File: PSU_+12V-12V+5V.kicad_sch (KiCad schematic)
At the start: 39 parts, among them Q1 BC557, Q2 BC557, Q3 BC547, Q4 BC547, U1 LM317L, U2 LM317L

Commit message: ...
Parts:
- added J1: Screw_Terminal_01x06, TerminalBlock_Phoenix:TerminalBlock_Phoenix_MKDS-1,5-6_1x06_P5.00mm_Horizontal, symbol Connector:Screw_Terminal_01x06
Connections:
- net at C13.1, D5.2 (A), D7.1 (K)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: now also J1.1 (Pin_1)
- net at C11.2, C13.2, C3.2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: now also J1.2 (Pin_2)
- net at C10.2, C12.2, C14.2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: now also J1.4 (Pin_4)
- net at C14.1, D6.2 (A), D8.1 (K)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: now also J1.3 (Pin_3)
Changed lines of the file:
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@@
   (junction (at 93.345 118.11) (diameter 0) (color 0 0 0 0)
   )
+  (junction (at 153.67 78.105) (diameter 0) (color 0 0 0 0)
+  )
   (junction (at 127.635 78.105) (diameter 0) (color 0 0 0 0)
   )
+  (junction (at 153.67 40.64) (diameter 0) (color 0 0 0 0)
+  )
   (junction (at 84.455 128.27) (diameter 0) (color 0 0 0 0)
   )
@@
   (junction (at 105.41 110.49) (diameter 0) (color 0 0 0 0)
   )
+  (junction (at 153.67 147.955) (diameter 0) (color 0 0 0 0)
+  )
   (junction (at 136.525 128.27) (diameter 0) (color 0 0 0 0)
   )
@@
   (junction (at 114.935 40.64) (diameter 0) (color 0 0 0 0)
   )
+  (junction (at 153.67 110.49) (diameter 0) (color 0 0 0 0)
+  )
   (junction (at 100.33 147.955) (diameter 0) (color 0 0 0 0)
   )
@@
     (stroke (width 0) (type default) (color 0 0 0 0))
   )
+  (wire (pts (xy 174.625 147.955) (xy 174.625 73.66))
+    (stroke (width 0) (type default) (color 0 0 0 0))
+  )
   (wire (pts (xy 76.2 95.25) (xy 76.2 87.63))
     (stroke (width 0) (type default) (color 0 0 0 0))
@@
     (stroke (width 0) (type default) (color 0 0 0 0))
   )
+  (wire (pts (xy 153.67 40.64) (xy 166.37 40.64))
+    (stroke (width 0) (type default) (color 0 0 0 0))
+  )
   (wire (pts (xy 106.68 139.065) (xy 106.68 147.955))
     (stroke (width 0) (type default) (color 0 0 0 0))
@@
     (stroke (width 0) (type default) (color 0 0 0 0))
   )
+  (wire (pts (xy 166.37 68.58) (xy 189.23 68.58))
+    (stroke (width 0) (type default) (color 0 0 0 0))
+  )
   (wire (pts (xy 114.935 147.955) (xy 127.635 147.955))
     (stroke (width 0) (type default) (color 0 0 0 0))
   )
+  (wire (pts (xy 166.37 66.04) (xy 189.23 66.04))
+    (stroke (width 0) (type default) (color 0 0 0 0))
+  )
   (wire (pts (xy 46.355 97.79) (xy 76.2 97.79))
     (stroke (width 0) (type default) (color 0 0 0 0))
@@
     (stroke (width 0) (type default) (color 0 0 0 0))
   )
+  (wire (pts (xy 169.545 110.49) (xy 169.545 71.12))
+    (stroke (width 0) (type default) (color 0 0 0 0))
+  )
   (wire (pts (xy 136.525 48.895) (xy 136.525 40.64))
     (stroke (width 0) (type default) (color 0 0 0 0))
@@
     (stroke (width 0) (type default) (color 0 0 0 0))
   )
+  (wire (pts (xy 174.625 73.66) (xy 189.23 73.66))
+    (stroke (width 0) (type default) (color 0 0 0 0))
+  )
   (wire (pts (xy 106.68 147.955) (xy 114.935 147.955))
     (stroke (width 0) (type default) (color 0 0 0 0))
@@
     (stroke (width 0) (type default) (color 0 0 0 0))
   )
+  (wire (pts (xy 153.67 110.49) (xy 169.545 110.49))
+    (stroke (width 0) (type default) (color 0 0 0 0))
+  )
   (wire (pts (xy 46.355 105.41) (xy 60.96 105.41))
     (stroke (width 0) (type default) (color 0 0 0 0))
   )
+  (wire (pts (xy 153.67 78.105) (xy 166.37 78.105))
+    (stroke (width 0) (type default) (color 0 0 0 0))
+  )
   (wire (pts (xy 46.355 95.25) (xy 76.2 95.25))
     (stroke (width 0) (type default) (color 0 0 0 0))
@@
     (stroke (width 0) (type default) (color 0 0 0 0))
   )
+  (wire (pts (xy 166.37 78.105) (xy 166.37 68.58))
+    (stroke (width 0) (type default) (color 0 0 0 0))
+  )
+  (wire (pts (xy 169.545 71.12) (xy 189.23 71.12))
+    (stroke (width 0) (type default) (color 0 0 0 0))
+  )
   (wire (pts (xy 127.635 128.27) (xy 136.525 128.27))
     (stroke (width 0) (type default) (color 0 0 0 0))
@@
     (stroke (width 0) (type default) (color 0 0 0 0))
   )
+  (wire (pts (xy 153.67 147.955) (xy 174.625 147.955))
+    (stroke (width 0) (type default) (color 0 0 0 0))
+  )
   (wire (pts (xy 106.68 58.42) (xy 106.68 64.135))
     (stroke (width 0) (type default) (color 0 0 0 0))
@@
   )
   (wire (pts (xy 114.935 78.105) (xy 127.635 78.105))
+    (stroke (width 0) (type default) (color 0 0 0 0))
+  )
+  (wire (pts (xy 166.37 40.64) (xy 166.37 66.04))
     (stroke (width 0) (type default) (color 0 0 0 0))
   )
@@
     (pin "2")
   )
+  (symbol (lib_id "Connector:Screw_Terminal_01x06") (at 194.31 71.12 0) (unit 1)
+    (in_bom yes) (on_board yes) (fields_autoplaced)
+    (property "Reference" "J1" (id 0) (at 196.85 71.1199 0)
+      (effects (font (size 1.27 1.27)) (justify left))
+    )
+    (property "Value" "Screw_Terminal_01x06" (id 1) (at 196.85 73.6599 0)
+      (effects (font (size 1.27 1.27)) (justify left))
+    )
+    (property "Footprint" "TerminalBlock_Phoenix:TerminalBlock_Phoenix_MKDS-1,5-6_1x06_P5.00mm_Horizontal" (id 2) (at 194.31 71.12 0)
+      (effects (font (size 1.27 1.27)) hide)
+    )
+    (property "Datasheet" "~" (id 3) (at 194.31 71.12 0)
+      (effects (font (size 1.27 1.27)) hide)
+    )
+    (pin "1")
+    (pin "2")
+    (pin "3")
+    (pin "4")
+    (pin "5")
+    (pin "6")
+  )
   (symbol (lib_id "Device:R_Small") (at 106.68 66.675 180) (unit 1)
     (in_bom yes) (on_board yes)
@@
       (reference "D8") (unit 1) (value "1N4004") (footprint "Diode_THT:D_DO-41_SOD81_P10.16mm_Horizontal")
     )
+    (path "/c78bdea5-e185-4052-a5d1-0feec00b8a09"
+      (reference "J1") (unit 1) (value "Screw_Terminal_01x06") (footprint "TerminalBlock_Phoenix:TerminalBlock_Phoenix_MKDS-1,5-6_1x06_P5.00mm_Horizontal")
+    )
     (path "/961e5191-6ef0-485b-8715-bf0eec14a118"

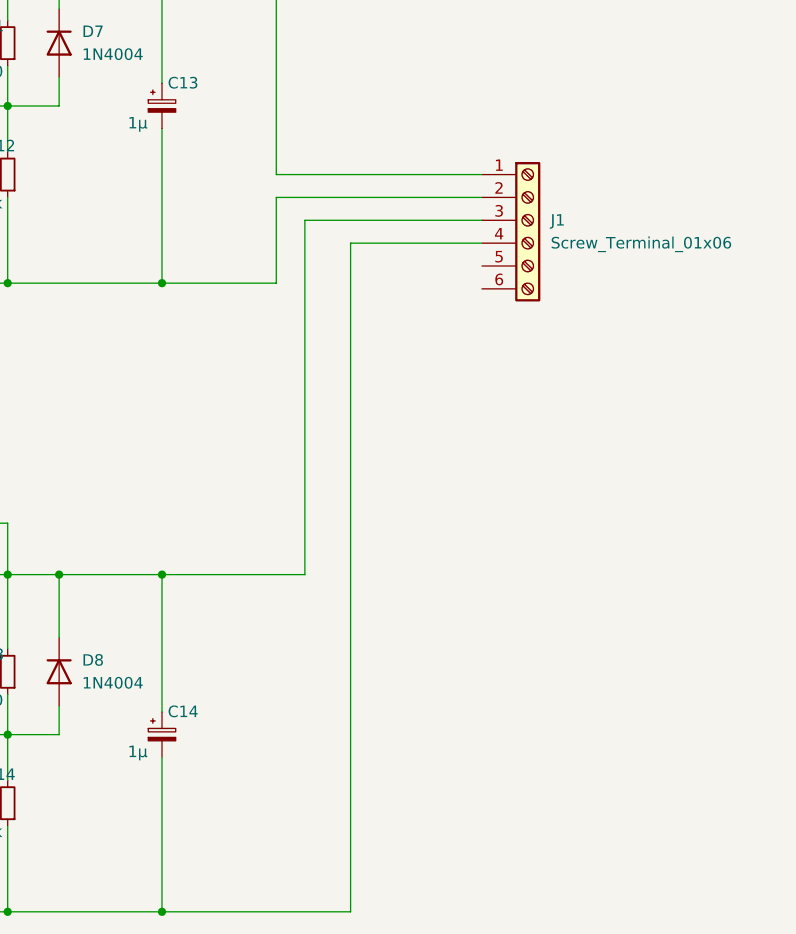
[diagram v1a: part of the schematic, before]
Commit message: Herschikkingen om filled area te optimaizeren
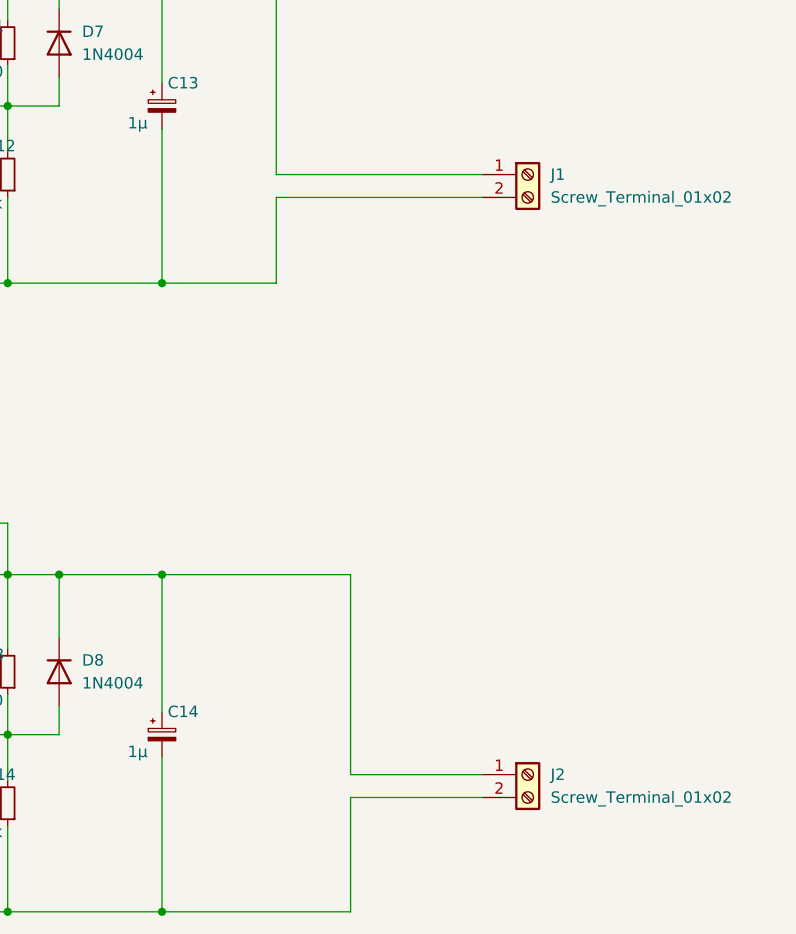
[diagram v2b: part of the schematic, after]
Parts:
- removed J1: Screw_Terminal_01x06, TerminalBlock_Phoenix:TerminalBlock_Phoenix_MKDS-1,5-6_1x06_P5.00mm_Horizontal, symbol Connector:Screw_Terminal_01x06
- added J1, J2: Screw_Terminal_01x02, TerminalBlock_Phoenix:TerminalBlock_Phoenix_MKDS-1,5-2_1x02_P5.00mm_Horizontal, symbol Connector:Screw_Terminal_01x02
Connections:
- net at C13.1, D5.2 (A), D7.1 (K)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: now also J1.1 (Pin_1)
- net at C11.2, C13.2, C3.2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: now also J1.2 (Pin_2)
- net at C10.2, C12.2, C14.2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: now also J2.2 (Pin_2)
- net at C14.1, D6.2 (A), D8.1 (K)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: now also J2.1 (Pin_1)
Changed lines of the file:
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@@
+    (stroke (width 0) (type default) (color 0 0 0 0))
+  )
+  (wire (pts (xy 174.625 132.715) (xy 174.625 110.49))
     (stroke (width 0) (type default) (color 0 0 0 0))
   )
@@
     (stroke (width 0) (type default) (color 0 0 0 0))
   )
-  (wire (pts (xy 174.625 147.955) (xy 174.625 73.66))
-    (stroke (width 0) (type default) (color 0 0 0 0))
-  )
   (wire (pts (xy 76.2 95.25) (xy 76.2 87.63))
     (stroke (width 0) (type default) (color 0 0 0 0))
@@
     (stroke (width 0) (type default) (color 0 0 0 0))
   )
+  (wire (pts (xy 174.625 147.955) (xy 174.625 135.255))
+    (stroke (width 0) (type default) (color 0 0 0 0))
+  )
   (wire (pts (xy 106.68 139.065) (xy 106.68 147.955))
     (stroke (width 0) (type default) (color 0 0 0 0))
@@
     (stroke (width 0) (type default) (color 0 0 0 0))
   )
-  (wire (pts (xy 169.545 110.49) (xy 169.545 71.12))
-    (stroke (width 0) (type default) (color 0 0 0 0))
-  )
   (wire (pts (xy 136.525 48.895) (xy 136.525 40.64))
     (stroke (width 0) (type default) (color 0 0 0 0))
@@
     (stroke (width 0) (type default) (color 0 0 0 0))
   )
-  (wire (pts (xy 174.625 73.66) (xy 189.23 73.66))
+  (wire (pts (xy 189.23 132.715) (xy 174.625 132.715))
     (stroke (width 0) (type default) (color 0 0 0 0))
   )
@@
     (stroke (width 0) (type default) (color 0 0 0 0))
   )
-  (wire (pts (xy 153.67 110.49) (xy 169.545 110.49))
+  (wire (pts (xy 153.67 110.49) (xy 174.625 110.49))
     (stroke (width 0) (type default) (color 0 0 0 0))
   )
@@
     (stroke (width 0) (type default) (color 0 0 0 0))
   )
-  (wire (pts (xy 169.545 71.12) (xy 189.23 71.12))
-    (stroke (width 0) (type default) (color 0 0 0 0))
-  )
   (wire (pts (xy 127.635 128.27) (xy 136.525 128.27))
     (stroke (width 0) (type default) (color 0 0 0 0))
@@
   )
   (wire (pts (xy 153.67 147.955) (xy 136.525 147.955))
+    (stroke (width 0) (type default) (color 0 0 0 0))
+  )
+  (wire (pts (xy 174.625 135.255) (xy 189.23 135.255))
     (stroke (width 0) (type default) (color 0 0 0 0))
   )
@@
     )
     (property "Datasheet" "http://www.vishay.com/docs/88503/1n4001.pdf" (id 3) (at 142.24 121.285 0)
+      (effects (font (size 1.27 1.27)) hide)
+    )
+    (pin "1")
+    (pin "2")
+  )
+  (symbol (lib_id "Connector:Screw_Terminal_01x02") (at 194.31 66.04 0) (unit 1)
+    (in_bom yes) (on_board yes) (fields_autoplaced)
+    (property "Reference" "J1" (id 0) (at 196.85 66.0399 0)
+      (effects (font (size 1.27 1.27)) (justify left))
+    )
+    (property "Value" "Screw_Terminal_01x02" (id 1) (at 196.85 68.5799 0)
+      (effects (font (size 1.27 1.27)) (justify left))
+    )
+    (property "Footprint" "TerminalBlock_Phoenix:TerminalBlock_Phoenix_MKDS-1,5-2_1x02_P5.00mm_Horizontal" (id 2) (at 194.31 66.04 0)
+      (effects (font (size 1.27 1.27)) hide)
+    )
+    (property "Datasheet" "~" (id 3) (at 194.31 66.04 0)
       (effects (font (size 1.27 1.27)) hide)
     )
@@
     (pin "2")
   )
-  (symbol (lib_id "Connector:Screw_Terminal_01x06") (at 194.31 71.12 0) (unit 1)
-    (in_bom yes) (on_board yes) (fields_autoplaced)
-    (property "Reference" "J1" (id 0) (at 196.85 71.1199 0)
-      (effects (font (size 1.27 1.27)) (justify left))
-    )
-    (property "Value" "Screw_Terminal_01x06" (id 1) (at 196.85 73.6599 0)
-      (effects (font (size 1.27 1.27)) (justify left))
-    )
-    (property "Footprint" "TerminalBlock_Phoenix:TerminalBlock_Phoenix_MKDS-1,5-6_1x06_P5.00mm_Horizontal" (id 2) (at 194.31 71.12 0)
-      (effects (font (size 1.27 1.27)) hide)
-    )
-    (property "Datasheet" "~" (id 3) (at 194.31 71.12 0)
-      (effects (font (size 1.27 1.27)) hide)
-    )
-    (pin "1")
-    (pin "2")
-    (pin "3")
-    (pin "4")
-    (pin "5")
-    (pin "6")
-  )
   (symbol (lib_id "Device:R_Small") (at 106.68 66.675 180) (unit 1)
     (in_bom yes) (on_board yes)
@@
     (pin "4")
   )
+  (symbol (lib_id "Connector:Screw_Terminal_01x02") (at 194.31 132.715 0) (unit 1)
+    (in_bom yes) (on_board yes) (fields_autoplaced)
+    (property "Reference" "J2" (id 0) (at 196.85 132.7149 0)
+      (effects (font (size 1.27 1.27)) (justify left))
+    )
+    (property "Value" "Screw_Terminal_01x02" (id 1) (at 196.85 135.2549 0)
+      (effects (font (size 1.27 1.27)) (justify left))
+    )
+    (property "Footprint" "TerminalBlock_Phoenix:TerminalBlock_Phoenix_MKDS-1,5-2_1x02_P5.00mm_Horizontal" (id 2) (at 194.31 132.715 0)
+      (effects (font (size 1.27 1.27)) hide)
+    )
+    (property "Datasheet" "~" (id 3) (at 194.31 132.715 0)
+      (effects (font (size 1.27 1.27)) hide)
+    )
+    (pin "1")
+    (pin "2")
+  )
   (sheet_instances
     (path "/" (page "1"))
@@
       (reference "D8") (unit 1) (value "1N4004") (footprint "Diode_THT:D_DO-41_SOD81_P10.16mm_Horizontal")
     )
-    (path "/c78bdea5-e185-4052-a5d1-0feec00b8a09"
-      (reference "J1") (unit 1) (value "Screw_Terminal_01x06") (footprint "TerminalBlock_Phoenix:TerminalBlock_Phoenix_MKDS-1,5-6_1x06_P5.00mm_Horizontal")
+    (path "/267aca1d-0cf0-41ab-8780-187b83e1d640"
+      (reference "J1") (unit 1) (value "Screw_Terminal_01x02") (footprint "TerminalBlock_Phoenix:TerminalBlock_Phoenix_MKDS-1,5-2_1x02_P5.00mm_Horizontal")
+    )
+    (path "/fb330b82-4564-4ce8-a441-9246ae0dc7d6"
+      (reference "J2") (unit 1) (value "Screw_Terminal_01x02") (footprint "TerminalBlock_Phoenix:TerminalBlock_Phoenix_MKDS-1,5-2_1x02_P5.00mm_Horizontal")
     )
     (path "/961e5191-6ef0-485b-8715-bf0eec14a118"

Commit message: Some shifting
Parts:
- J1: value Screw_Terminal_01x02 -> PSU12a
- J2: value Screw_Terminal_01x02 -> PSU12b
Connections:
- net 12Va: now reaches C13.1, D5.2 (A), D7.1 (K), J1.1 (Pin_1), R11.2, U1.2 (VO)
- net 0Va: now reaches C11.2, C13.2, C3.2, C7.2, C9.2, D1.2 (-), J1.2 (Pin_2), R12.1, R9.1
- net 0Vb: now reaches C10.2, C12.2, C14.2, C4.2, C5.2, D2.2 (-), J2.2 (Pin_2), R14.1, R6.1
- net 12Vb: now reaches C14.1, D6.2 (A), D8.1 (K), J2.1 (Pin_1), R13.2, U2.2 (VO)
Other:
- moved on the sheet: C1, C10, C11, C12, C13, C14, C2, C3, C4, C5, C7, C9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
